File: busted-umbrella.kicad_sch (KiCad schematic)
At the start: 44 parts, among them J1 SWD, J2 DB9_Male, M1 USB_B, SW1 TL2201, U1 ATSAME51J18A-MF, U2 LM3940IMP-3.3_SOT223, U3 CRV2S0505SC, U4 ADM3058E, Y1 8MHz

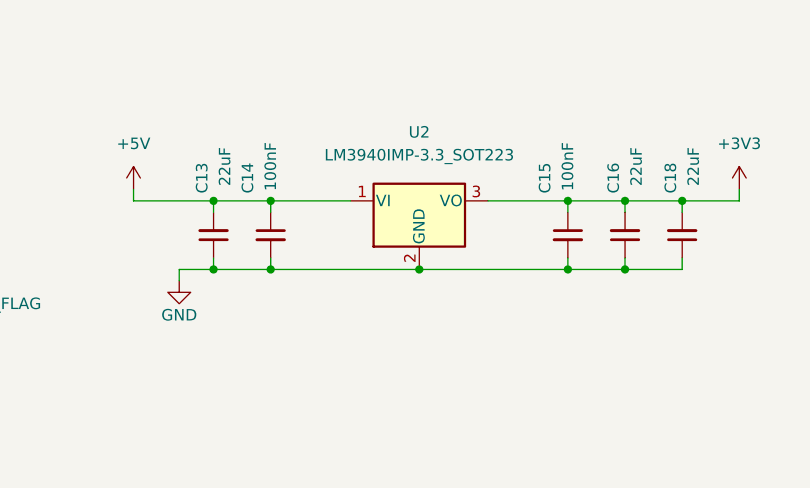
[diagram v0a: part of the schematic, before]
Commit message: changed ldo
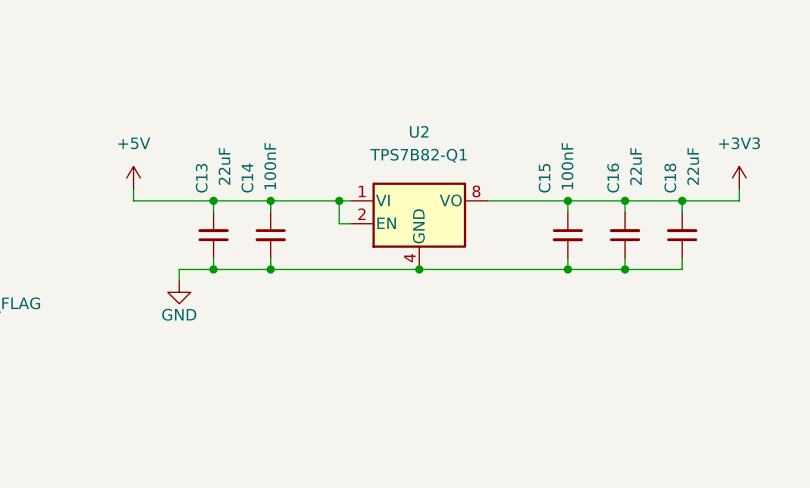
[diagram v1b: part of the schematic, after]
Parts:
- removed U2: LM3940IMP-3.3_SOT223, Package_TO_SOT_SMD:SOT-223-3_TabPin2, symbol ownLib:LM3940IMP-3.3_SOT223
- added U2: TPS7B82-Q1, Package_SO:Texas_R-PDSO-G8_EP2.95x4.9mm_Mask2.4x3.1mm, symbol ownLib:TPS7B82-Q1
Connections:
- net +3V3: now also U2.8 (VO)
- net +5V: now also U2.1 (VI), U2.2 (EN)
- net GND: now also U2.3 (GND), U2.4 (GND), U2.5 (GND), U2.6 (GND), U2.7 (GND), U2.9 (GND)
